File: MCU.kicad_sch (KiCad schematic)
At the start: 32 parts, among them J1 USB_C_Receptacle_USB2.0_14P, SW1 BOOT0, U1 STM32F722RETx, U2 AMS1117-3.3, X2 32.768kHz 7pF, Y1 16MHz 10pF

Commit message: Updated schematic with parts found in JLCPCB parts database. Updated footprints, 3d models for those items. All schematic symbols now have LCSC part numbers, footprints and 3D models. No PCB layout has been done.
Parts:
- removed J1: USB_C_Receptacle_USB2.0_14P, Connector_USB:USB_C_Receptacle_HRO_TYPE-C-31-M-12, symbol Connector:USB_C_Receptacle_USB2.0_14P
- removed X2: 32.768kHz 7pF, PCM_Crystal_AKL:Crystal_SMD_3215-2Pin_3.2x1.5mm, symbol PCM_Crystal_AKL:SMD3215-2
- added J1: GT-USB-7010I, easyeda2kicad:USB-C-SMD_GT-USB-7010I, symbol easyeda2kicad:GT-USB-7010I
- added X1: 32.768kHz 7pF, easyeda2kicad:FC-135R_L3.2-W1.5, symbol easyeda2kicad:Q13FC1350000200
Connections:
- net GND: now also J1.A1B12 (GND), J1.B1A12 (GND)
- net RCC_OSC32_IN: now also X1.1
- net RCC_OSC32_OUT: now also X1.2
- net USB_OTG_FS_D+: now also J1.A6 (D1+), J1.B6 (D+)
- net USB_OTG_FS_D-: now also J1.A7 (D1-), J1.B7 (D-)
- net VBUS: now also J1.A4B9 (VBUS), J1.B4A9 (VBUS)
- net at R2.2: now also J1.B5 (CC2)
- net at R3.2: now also J1.A5 (CC1)
- no-connect marks 1 -> 7
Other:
- note added: "TODO: Shield ground should NOT be connected to regular ground"
- note removed: "TODO: Shield to ground protection"
- moved on the sheet: R2, R3

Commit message: Group PCB components together more. Replace 2x2x4 by 1x2x8 connector.
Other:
- note added: "Decoupling Capacitors 1x 100nF per VDD/VBAT See DS11853 Rev 9 page 155"
- note removed: "1x 100nF per VDD/VBAT"
- note removed: "Bypass Capacitors"
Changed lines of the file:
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@@
 		)
 	)
-	(text "1x 100nF per VDD/VBAT"
+	(text "Decoupling Capacitors\n1x 100nF per VDD/VBAT\nSee DS11853 Rev 9 page 155"
 		(exclude_from_sim no)
-		(at 80.772 34.798 0)
+		(at 56.134 32.766 0)
 		(effects
 			(font
 				(size 1.27 1.27)
 			)
+			(justify left)
 		)
 	)
@@
 		(effects
 			(font
-				(size 1.27 1.27)
-			)
-		)
-	)
-	(text "Bypass Capacitors"
-		(exclude_from_sim no)
-		(at 77.724 32.258 0)
-		(effects
-			(font

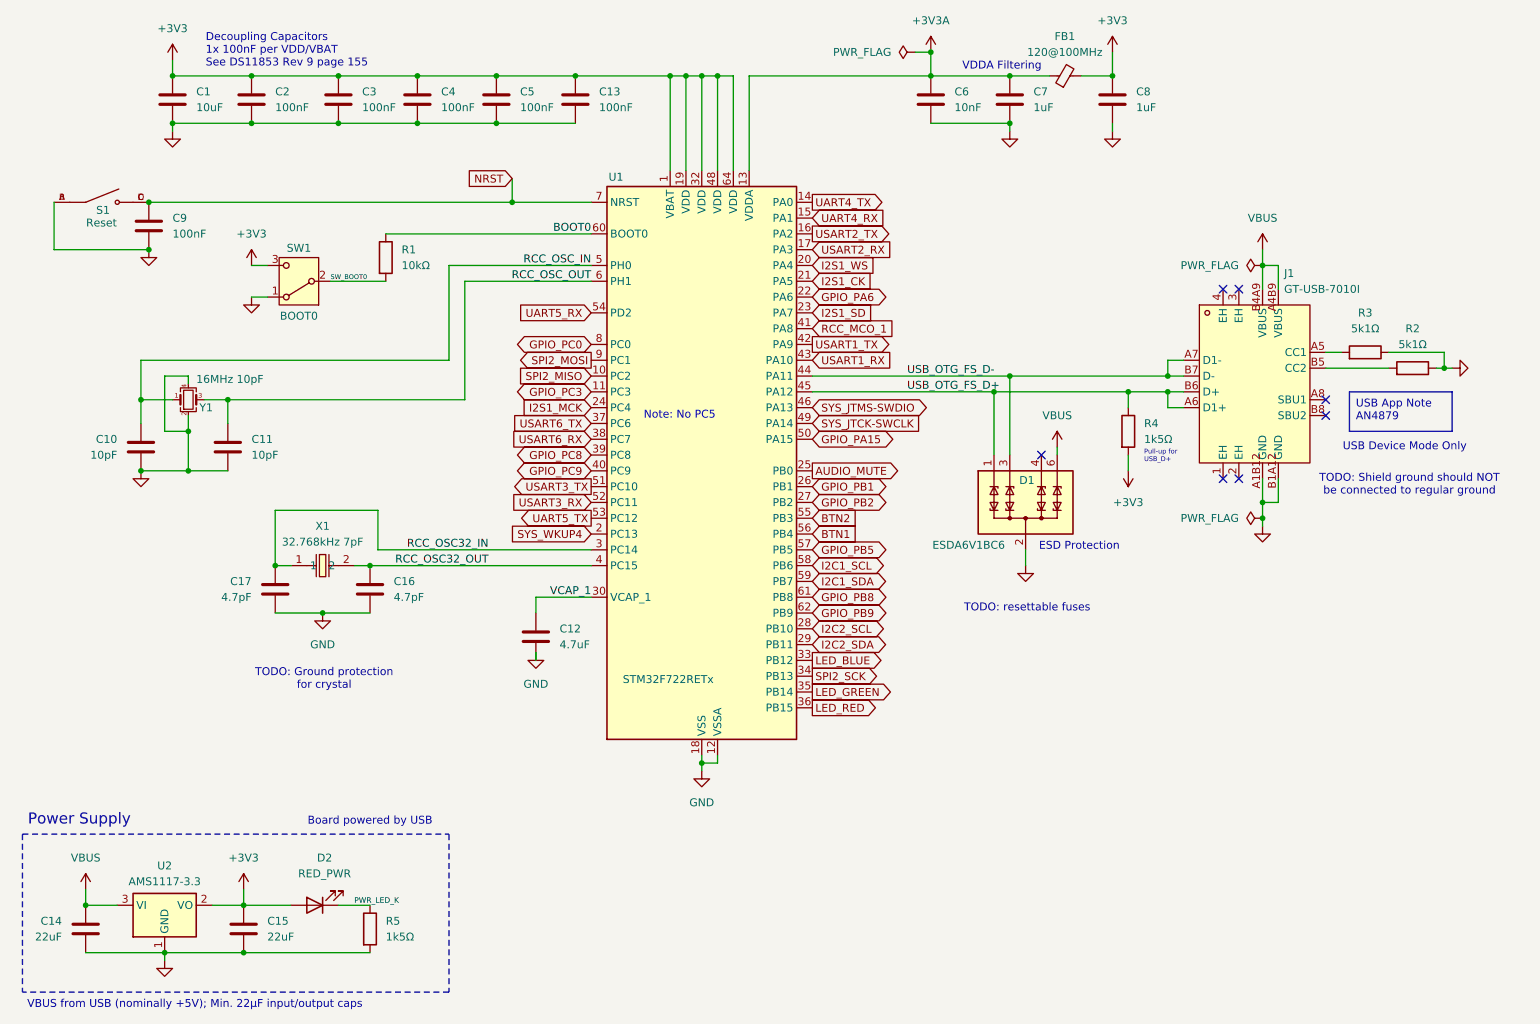
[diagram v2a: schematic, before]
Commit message: Create PCB outline and move components into better locations. (Not done yet!) Update schematic a little bit with additional nets and clarifications. Add mounting holes. Unify components/footprints.
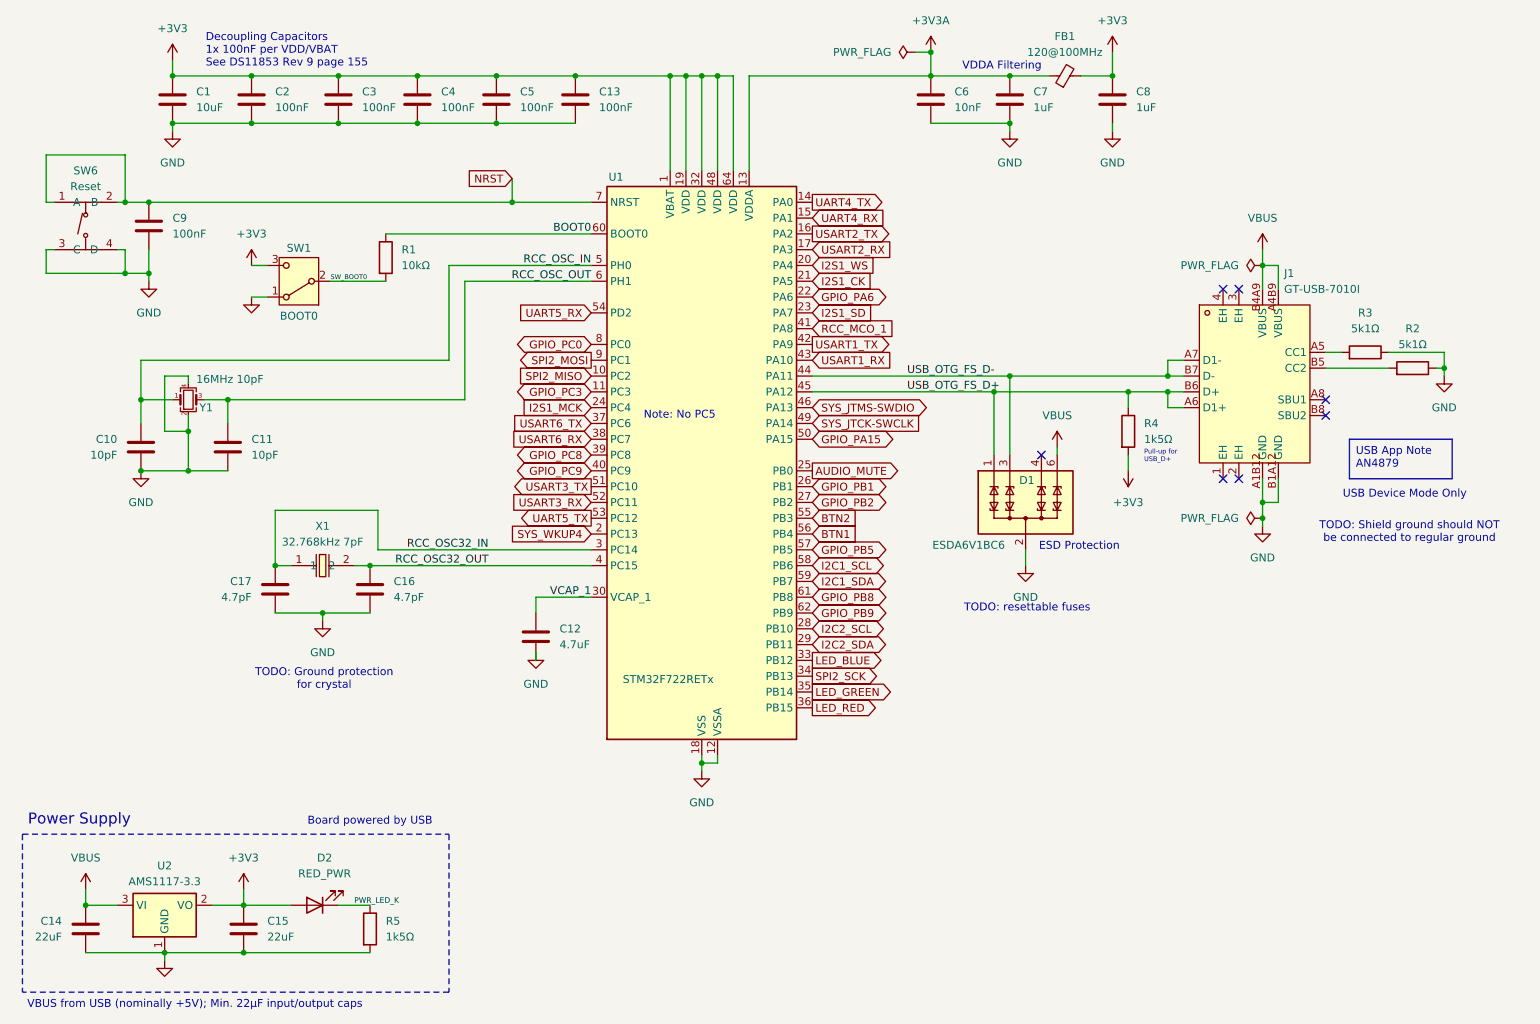
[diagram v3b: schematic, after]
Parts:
- removed S1: Reset, stm-midi-poc1:SW_TS-1187A-B-A-B, symbol TS-1187A-B-A-B:TS-1187A-B-A-B
- added SW6: Reset, easyeda2kicad:SW-SMD_4P-L5.1-W5.1-P3.70-LS6.5-TL-2, symbol easyeda2kicad:TS-1187A-B-A-B
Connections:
- net GND: now also SW6.3 (C), SW6.4 (D)
- net NRST: now also SW6.1 (A), SW6.2 (B)

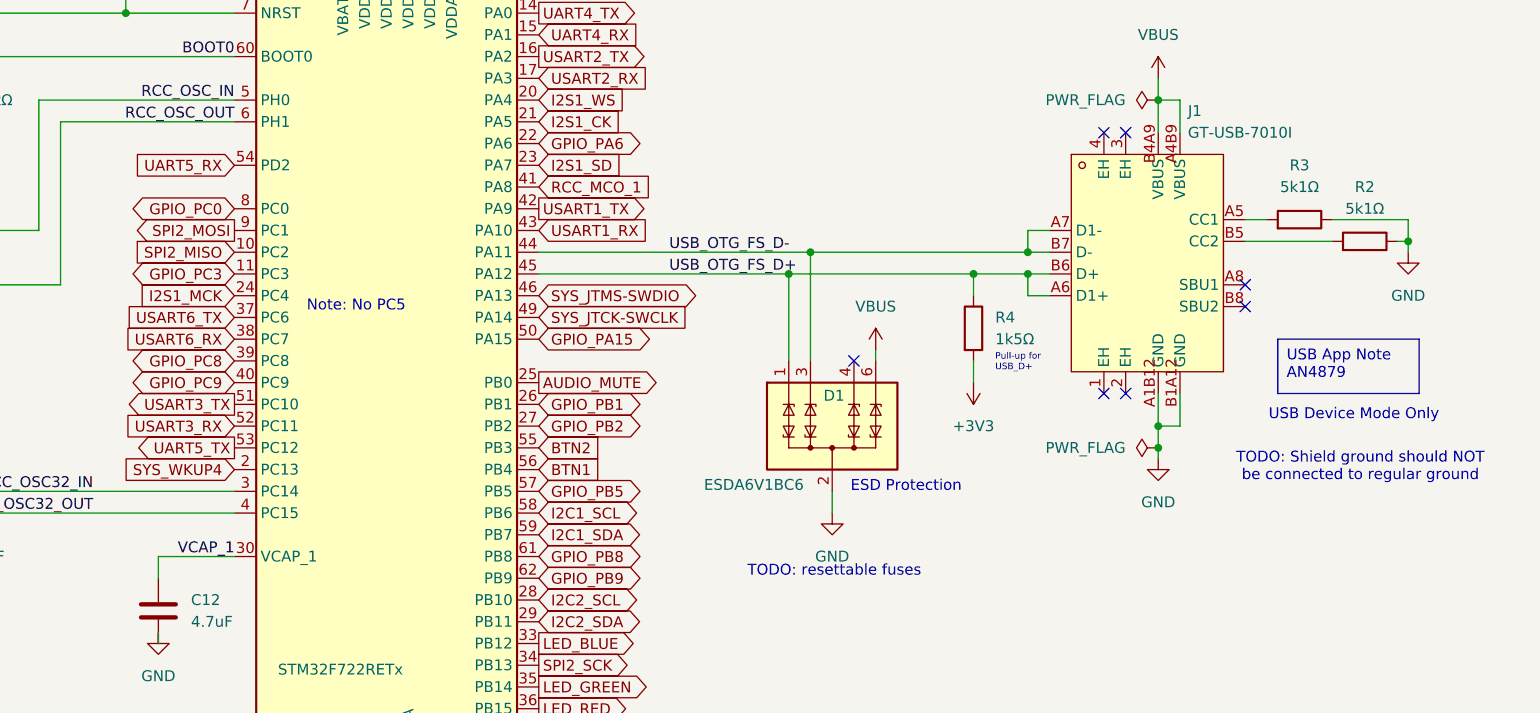
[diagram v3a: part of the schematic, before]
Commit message: Connected all power for Decoupling Caps
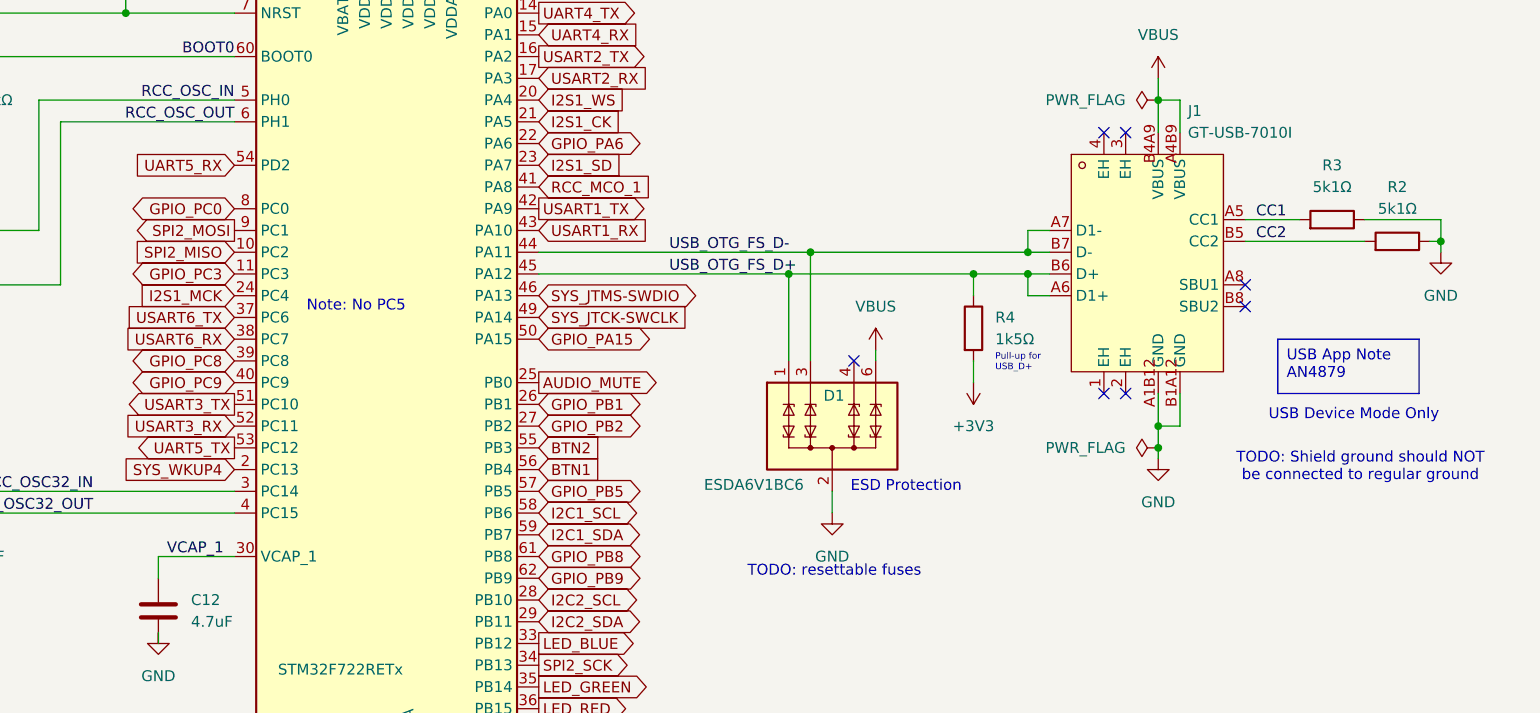
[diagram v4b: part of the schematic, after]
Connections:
- net CC2: now reaches J1.B5 (CC2), R2.2
- net CC1: now reaches J1.A5 (CC1), R3.2
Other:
- moved on the sheet: R2, R3
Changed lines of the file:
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@@
 	)
 	(junction
-		(at 255.27 83.82)
+		(at 259.08 83.82)
 		(diameter 0)
 		(color 0 0 0 0)
@@
 	(wire
 		(pts
-			(xy 255.27 81.28) (xy 255.27 83.82)
+			(xy 259.08 81.28) (xy 259.08 83.82)
 		)
 		(stroke
@@
 	(wire
 		(pts
-			(xy 255.27 83.82) (xy 254 83.82)
-		)
-		(stroke
-			(width 0)
-			(type default)
-		)
-	)
-	(wire
-		(pts
 			(xy 45.72 100.33) (xy 53.34 100.33)
 		)
@@
 	(wire
 		(pts
-			(xy 255.27 85.09) (xy 255.27 83.82)
+			(xy 259.08 85.09) (xy 259.08 83.82)
 		)
 		(stroke
@@
 	(wire
 		(pts
+			(xy 257.81 83.82) (xy 259.08 83.82)
+		)
+		(stroke
+			(width 0)
+			(type default)
+		)
+	)
+	(wire
+		(pts
 			(xy 143.51 36.83) (xy 172.72 36.83)
 		)
@@
 	(wire
 		(pts
-			(xy 238.76 81.28) (xy 236.22 81.28)
+			(xy 242.57 81.28) (xy 236.22 81.28)
 		)
 		(stroke
@@
 	(wire
 		(pts
-			(xy 246.38 81.28) (xy 255.27 81.28)
+			(xy 250.19 81.28) (xy 259.08 81.28)
 		)
 		(stroke
@@
 	(wire
 		(pts
-			(xy 118.11 120.65) (xy 109.22 120.65)
+			(xy 109.22 120.65) (xy 118.11 120.65)
 		)
 		(stroke
@@
 	(wire
 		(pts
-			(xy 246.38 83.82) (xy 236.22 83.82)
+			(xy 250.19 83.82) (xy 236.22 83.82)
 		)
 		(stroke
@@
 	)
 	(label "VCAP_1"
-		(at 118.11 120.65 180)
+		(at 116.84 120.65 180)
 		(fields_autoplaced yes)
 		(effects
@@
 		)
 	)
+	(label "CC2"
+		(at 237.49 83.82 0)
+		(fields_autoplaced yes)
+		(effects
+			(font
+				(size 1.27 1.27)
+			)
+			(justify left bottom)
+		)
+	)
 	(label "SW_BOOT0"
 		(at 76.2 69.85 0)
@@
 		)
 	)
+	(label "CC1"
+		(at 237.49 81.28 0)
+		(fields_autoplaced yes)
+		(effects
+			(font
+				(size 1.27 1.27)
+			)
+			(justify left bottom)
+		)
+	)
 	(label "USB_OTG_FS_D+"
 		(at 168.91 87.63 0)
@@
 	(symbol
 		(lib_id "Device:R")
-		(at 250.19 83.82 270)
+		(at 254 83.82 270)
 		(mirror x)
 		(unit 1)
@@
 		(fields_autoplaced yes)
 		(property "Reference" "R2"
-			(at 250.19 77.47 90)
+			(at 254 77.47 90)
 			(effects
 				(font
@@
 		)
 		(property "Value" "5k1Ω"
-			(at 250.19 80.01 90)
+			(at 254 80.01 90)
 			(effects
 				(font
@@
 		)
 		(property "Footprint" "Resistor_SMD:R_0402_1005Metric"
-			(at 250.19 85.598 90)
+			(at 254 85.598 90)
 			(effects
 				(font
@@
 		)
 		(property "Datasheet" "~"
-			(at 250.19 83.82 0)
+			(at 254 83.82 0)
 			(effects
 				(font
@@
 		)
 		(property "Description" "Resistor"
-			(at 250.19 83.82 0)
+			(at 254 83.82 0)
 			(effects
 				(font
@@
 		)
 		(property "LCSC" "C25905"
-			(at 250.19 83.82 0)
+			(at 254 83.82 0)
 			(effects
 				(font
@@
 		)
 		(property "DPFNOTES" ""
-			(at 250.19 83.82 0)
+			(at 254 83.82 0)
 			(effects
 				(font
@@
 		)
 		(property "DPFURL" ""
-			(at 250.19 83.82 0)
+			(at 254 83.82 0)
 			(effects
 				(font
@@
 	(symbol
 		(lib_id "Device:R")
-		(at 242.57 81.28 270)
+		(at 246.38 81.28 270)
 		(mirror x)
 		(unit 1)
@@
 		(fields_autoplaced yes)
 		(property "Reference" "R3"
-			(at 242.57 74.93 90)
+			(at 246.38 74.93 90)
 			(effects
 				(font
@@
 		)
 		(property "Value" "5k1Ω"
-			(at 242.57 77.47 90)
+			(at 246.38 77.47 90)
 			(effects
 				(font
@@
 		)
 		(property "Footprint" "Resistor_SMD:R_0402_1005Metric"
-			(at 242.57 83.058 90)
+			(at 246.38 83.058 90)
 			(effects
 				(font
@@
 		)
 		(property "Datasheet" "~"
-			(at 242.57 81.28 0)
+			(at 246.38 81.28 0)
 			(effects
 				(font
@@
 		)
 		(property "Description" "Resistor"
-			(at 242.57 81.28 0)
+			(at 246.38 81.28 0)
 			(effects
 				(font
@@
 		)
 		(property "LCSC" "C25905"
-			(at 242.57 81.28 0)
+			(at 246.38 81.28 0)
 			(effects
 				(font
@@
 		)
 		(property "DPFNOTES" ""
-			(at 242.57 81.28 0)
+			(at 246.38 81.28 0)
 			(effects
 				(font
@@
 		)
 		(property "DPFURL" ""
-			(at 242.57 81.28 0)
+			(at 246.38 81.28 0)
 			(effects
 				(font
@@
 	(symbol
 		(lib_id "power:GND")
-		(at 255.27 85.09 0)
+		(at 259.08 85.09 0)
 		(mirror y)
 		(unit 1)
@@
 		(fields_autoplaced yes)
 		(property "Reference" "#PWR012"
-			(at 255.27 91.44 0)
+			(at 259.08 91.44 0)
 			(effects
 				(font
@@
 		)
 		(property "Value" "GND"
-			(at 255.27 90.17 0)
+			(at 259.08 90.17 0)
 			(effects
 				(font
@@
 		)
 		(property "Footprint" ""
-			(at 255.27 85.09 0)
+			(at 259.08 85.09 0)
 			(effects
 				(font
@@
 		)
 		(property "Datasheet" ""
-			(at 255.27 85.09 0)
+			(at 259.08 85.09 0)
 			(effects
 				(font
@@
 		)
 		(property "Description" "Power symbol creates a global label with name \"GND\" , ground"
-			(at 255.27 85.09 0)
+			(at 259.08 85.09 0)
 			(effects
 				(font
@@
 		)
 		(property "LCSC" ""
-			(at 255.27 85.09 0)
+			(at 259.08 85.09 0)
 			(effects
 				(font
@@
 		)
 		(property "DPFNOTES" ""
-			(at 255.27 85.09 0)
+			(at 259.08 85.09 0)
 			(effects
 				(font
@@
 		)
 		(property "DPFURL" ""
-			(at 255.27 85.09 0)
+			(at 259.08 85.09 0)
 			(effects
 				(font
